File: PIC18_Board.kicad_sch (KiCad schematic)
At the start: 1 part

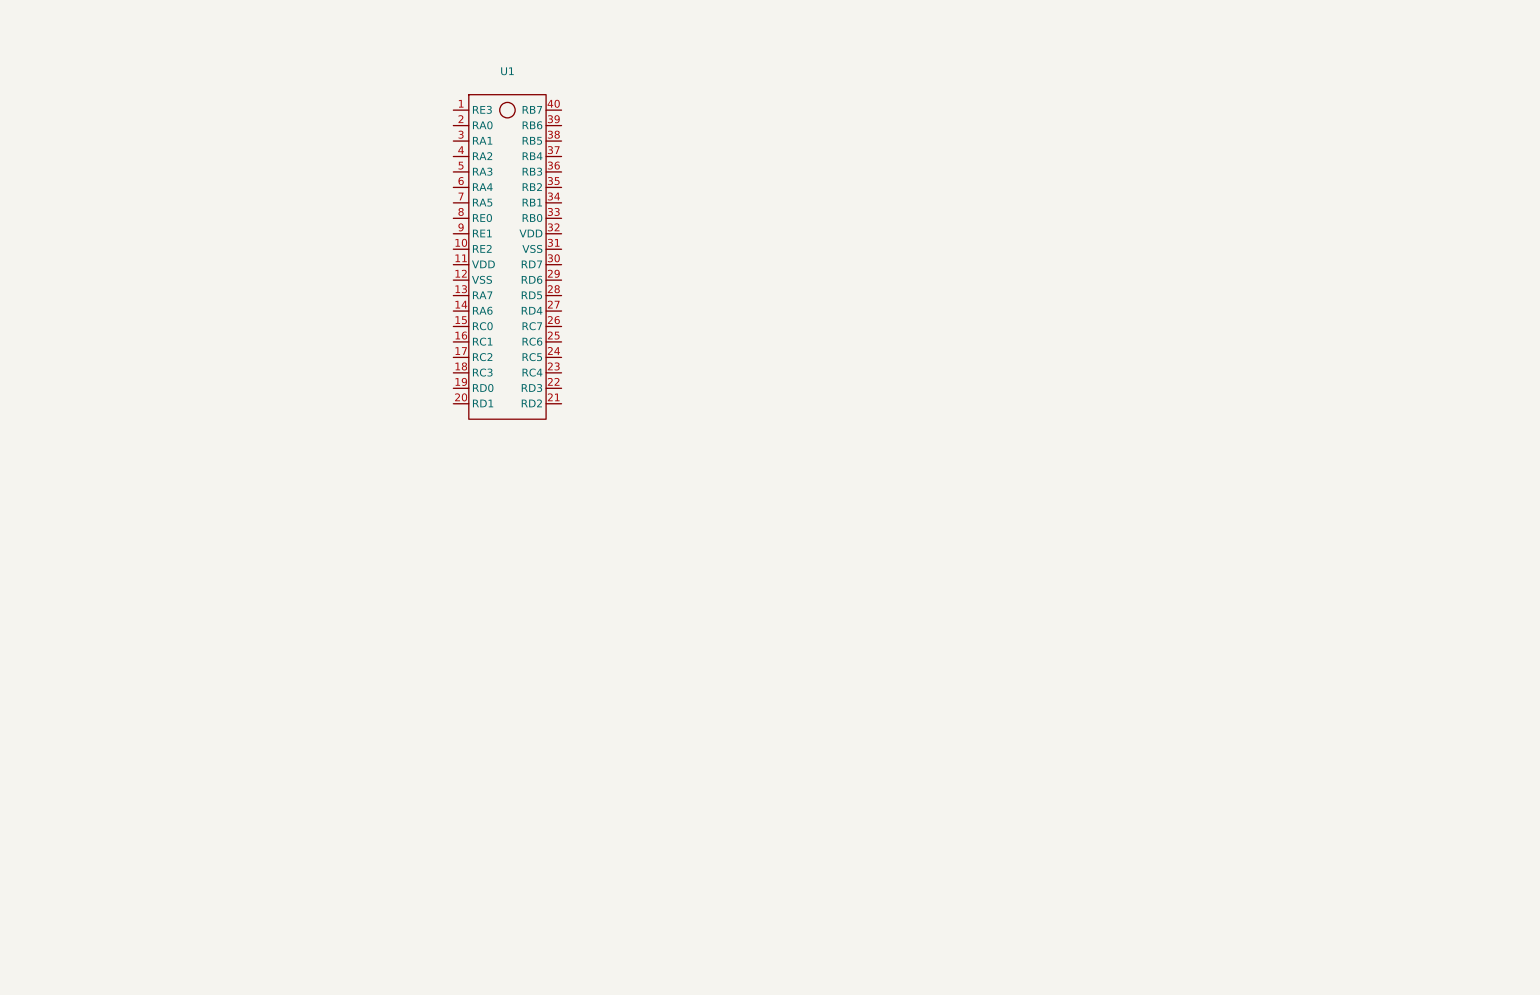
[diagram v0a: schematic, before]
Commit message: Add library,  first draft of ports
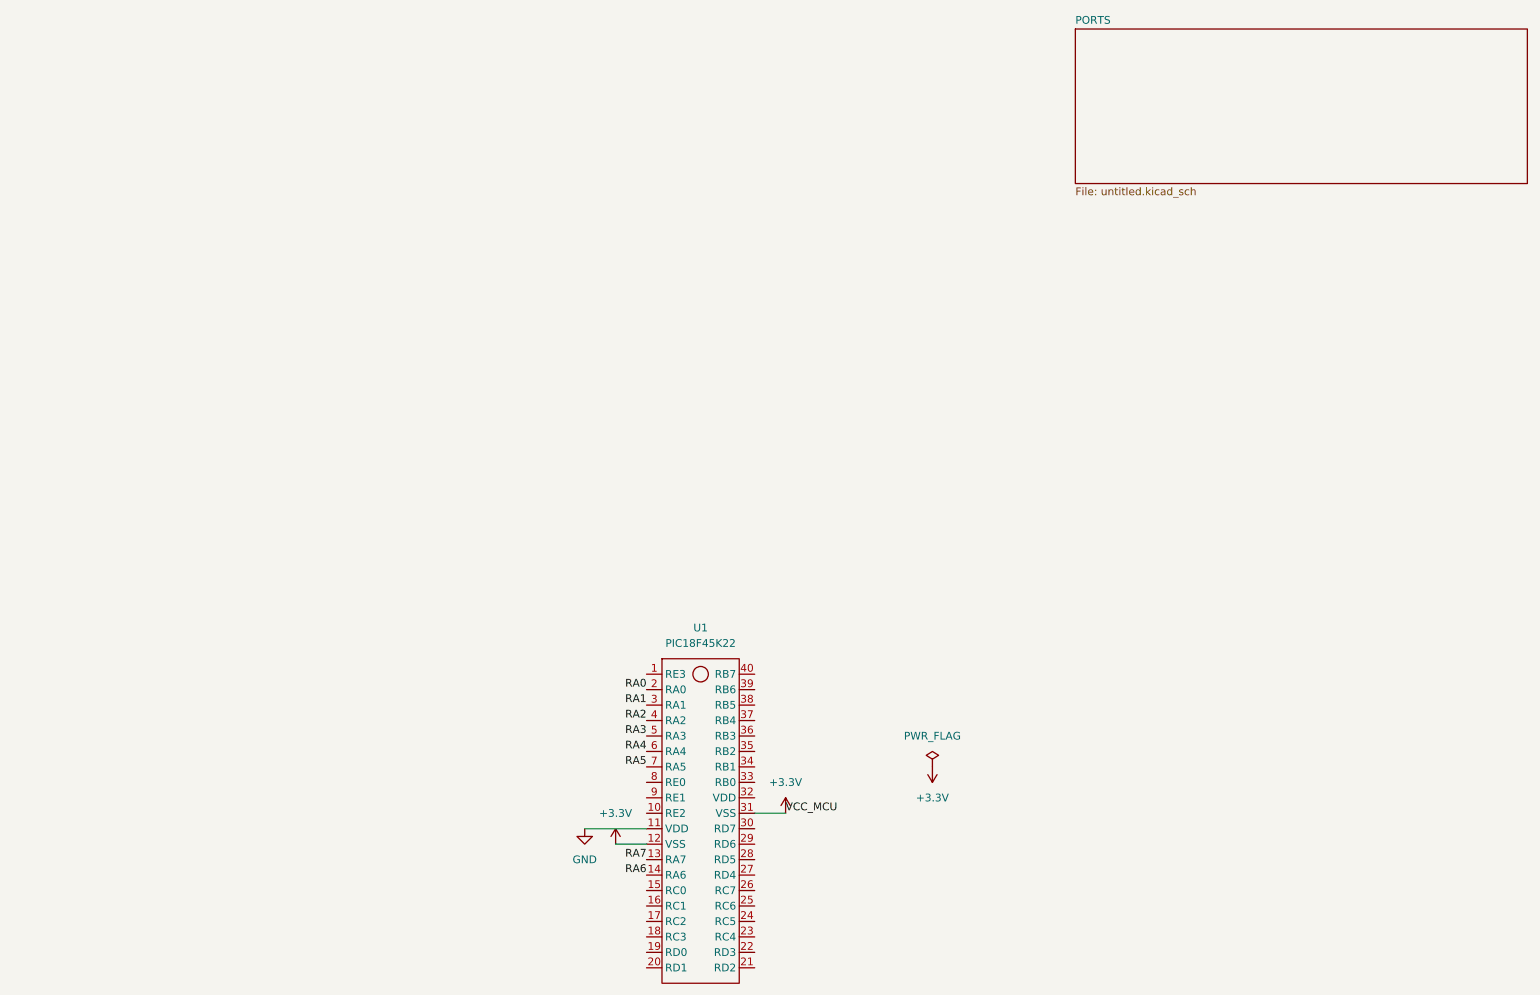
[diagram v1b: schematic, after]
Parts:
- U1: value ~ -> PIC18F45K22
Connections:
- net GND: now reaches U1.11 (VDD)
- net +3.3V: now reaches U1.12 (VSS)
- net +3.3V: now also U1.31 (VSS)
- net RA7: now reaches U1.13 (RA7)
- net RA6: now reaches U1.14 (RA6)
- net RA0: now reaches U1.2 (RA0)
- net RA1: now reaches U1.3 (RA1)
- net RA2: now reaches U1.4 (RA2)
- net RA3: now reaches U1.5 (RA3)
- net RA4: now reaches U1.6 (RA4)
- net RA5: now reaches U1.7 (RA5)
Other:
- added sheet PORTS (untitled.kicad_sch)
- moved on the sheet: U1

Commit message: Finalized PORTS
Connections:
- net GND: now also U1.32 (VDD)
- net RE3: now reaches U1.1 (RE3)
- net RE2: now reaches U1.10 (RE2)
- net RC0: now reaches U1.15 (RC0)
- net RC1: now reaches U1.16 (RC1)
- net RC2: now reaches U1.17 (RC2)
- net RC3: now reaches U1.18 (RC3)
- net RD0: now reaches U1.19 (RD0)
- net RD1: now reaches U1.20 (RD1)
- net RD2: now reaches U1.21 (RD2)
- net RD3: now reaches U1.22 (RD3)
- net RC4: now reaches U1.23 (RC4)
- net RC5: now reaches U1.24 (RC5)
- net RC6: now reaches U1.25 (RC6)
- net RC7: now reaches U1.26 (RC7)
- net RD4: now reaches U1.27 (RD4)
- net RD5: now reaches U1.28 (RD5)
- net RD6: now reaches U1.29 (RD6)
- net RD7: now reaches U1.30 (RD7)
- net RB0: now reaches U1.33 (RB0)
- net RB1: now reaches U1.34 (RB1)
- net RB2: now reaches U1.35 (RB2)
- net RB3: now reaches U1.36 (RB3)
- net RB4: now reaches U1.37 (RB4)
- net RB5: now reaches U1.38 (RB5)
- net RB6: now reaches U1.39 (RB6)
- net RB7: now reaches U1.40 (RB7)
- net RE0: now reaches U1.8 (RE0)
- net RE1: now reaches U1.9 (RE1)

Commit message: Feat: add power reg, usb protocol converter
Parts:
- added C3, C4: 4.7 uF, symbol Device:C_Small
- added J4: USB_B, symbol Connector:USB_B
- added J7: Conn_02x05_Odd_Even, Connector_PinSocket_2.54mm:PinSocket_2x05_P2.54mm_Vertical, symbol Connector_Generic:Conn_02x05_Odd_Even
- added R49: 10k, symbol Device:R_Small_US
- added U3: MCP2221AxML, Package_DFN_QFN:QFN-16-1EP_4x4mm_P0.65mm_EP2.5x2.5mm, symbol Interface_USB:MCP2221AxML
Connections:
- net +3.3V: now also U1.11 (VDD), U1.32 (VDD), J7.1 (Pin_1), J7.2 (Pin_2); no longer U1.12 (VSS), U1.31 (VSS)
- net GND: now also U1.12 (VSS), U1.31 (VSS), C3.2, C4.2, J4.4 (GND), J7.10 (Pin_10), J7.9 (Pin_9), U3.13 (VSS); no longer U1.11 (VDD), U1.32 (VDD)
- net RB6: now also J7.3 (Pin_3), J7.4 (Pin_4)
- net RB7: now also J7.5 (Pin_5), J7.6 (Pin_6)
- net RC6: now also U3.5 (UTx)
- net RC7: now also U3.4 (URx)
- new net: J4.2 (D-), U3.11 (D-)
- new net: J4.3 (D+), U3.12 (D+)
- new net: R49.2, U3.3 (~{RST})
- new net +5V: C4.1, J4.1 (VBUS), R49.1, U3.16 (VDD)
- new net MCLR: J7.8 (Pin_8)
- new net MCLR-MCU: J7.7 (Pin_7)
- new net VUSB: C3.1, U3.10 (VUSB)
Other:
- added sheet Power (Power_sch.kicad_sch)
- note added: "MikroProg collector"
